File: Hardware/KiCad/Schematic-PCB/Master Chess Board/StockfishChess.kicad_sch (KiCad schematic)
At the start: 70 parts, among them J1 ZF1-15-02-X-WT-X, J2 USB4110GFA, J4 ZF1-15-02-X-WT-X, J6 ZF1-15-02-X-WT-X, J8 ZF1-15-02-X-WT-X, SW2 SW_Omron_B3FS, U1 ESP32-S3-WROOM-2, U143 SN74AHCT125D, U144 USBLC6-2P6, U145 RUEF300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

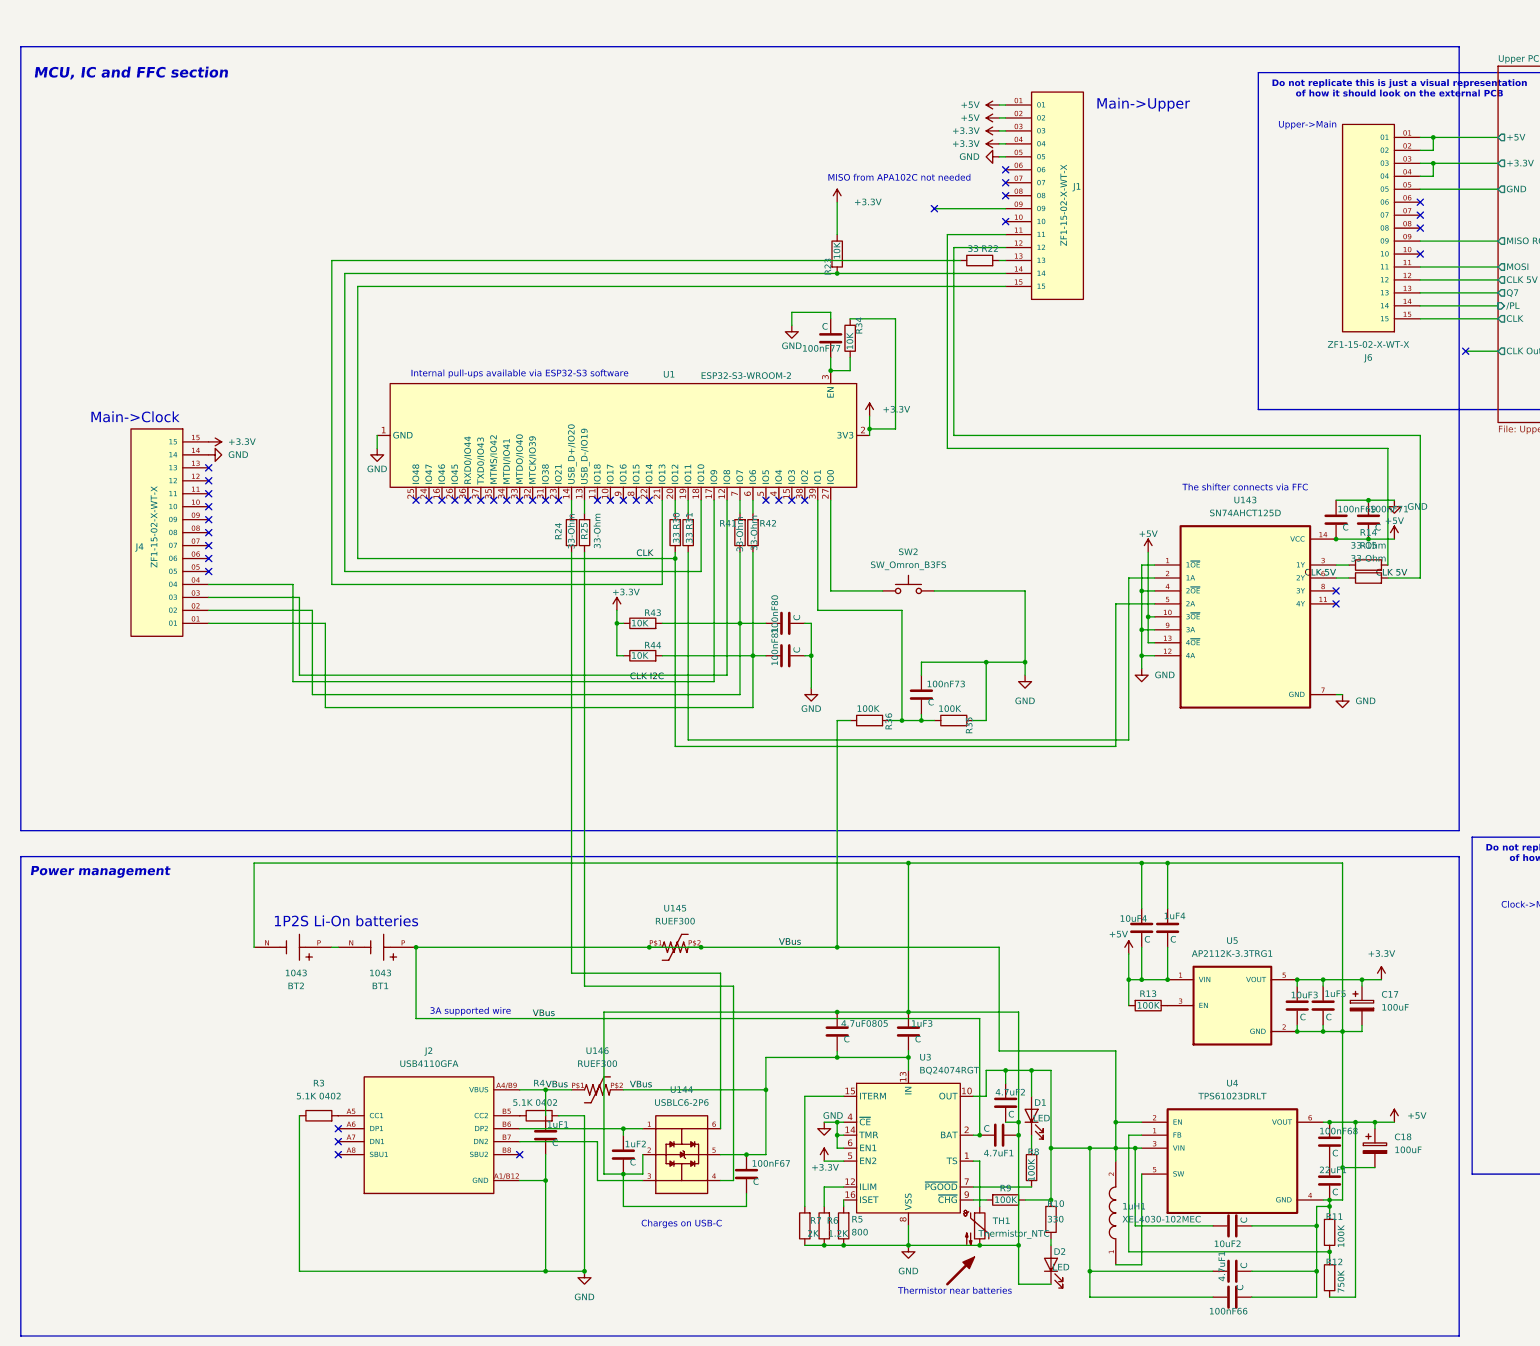
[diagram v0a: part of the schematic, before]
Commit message: Improved Schematic visuals
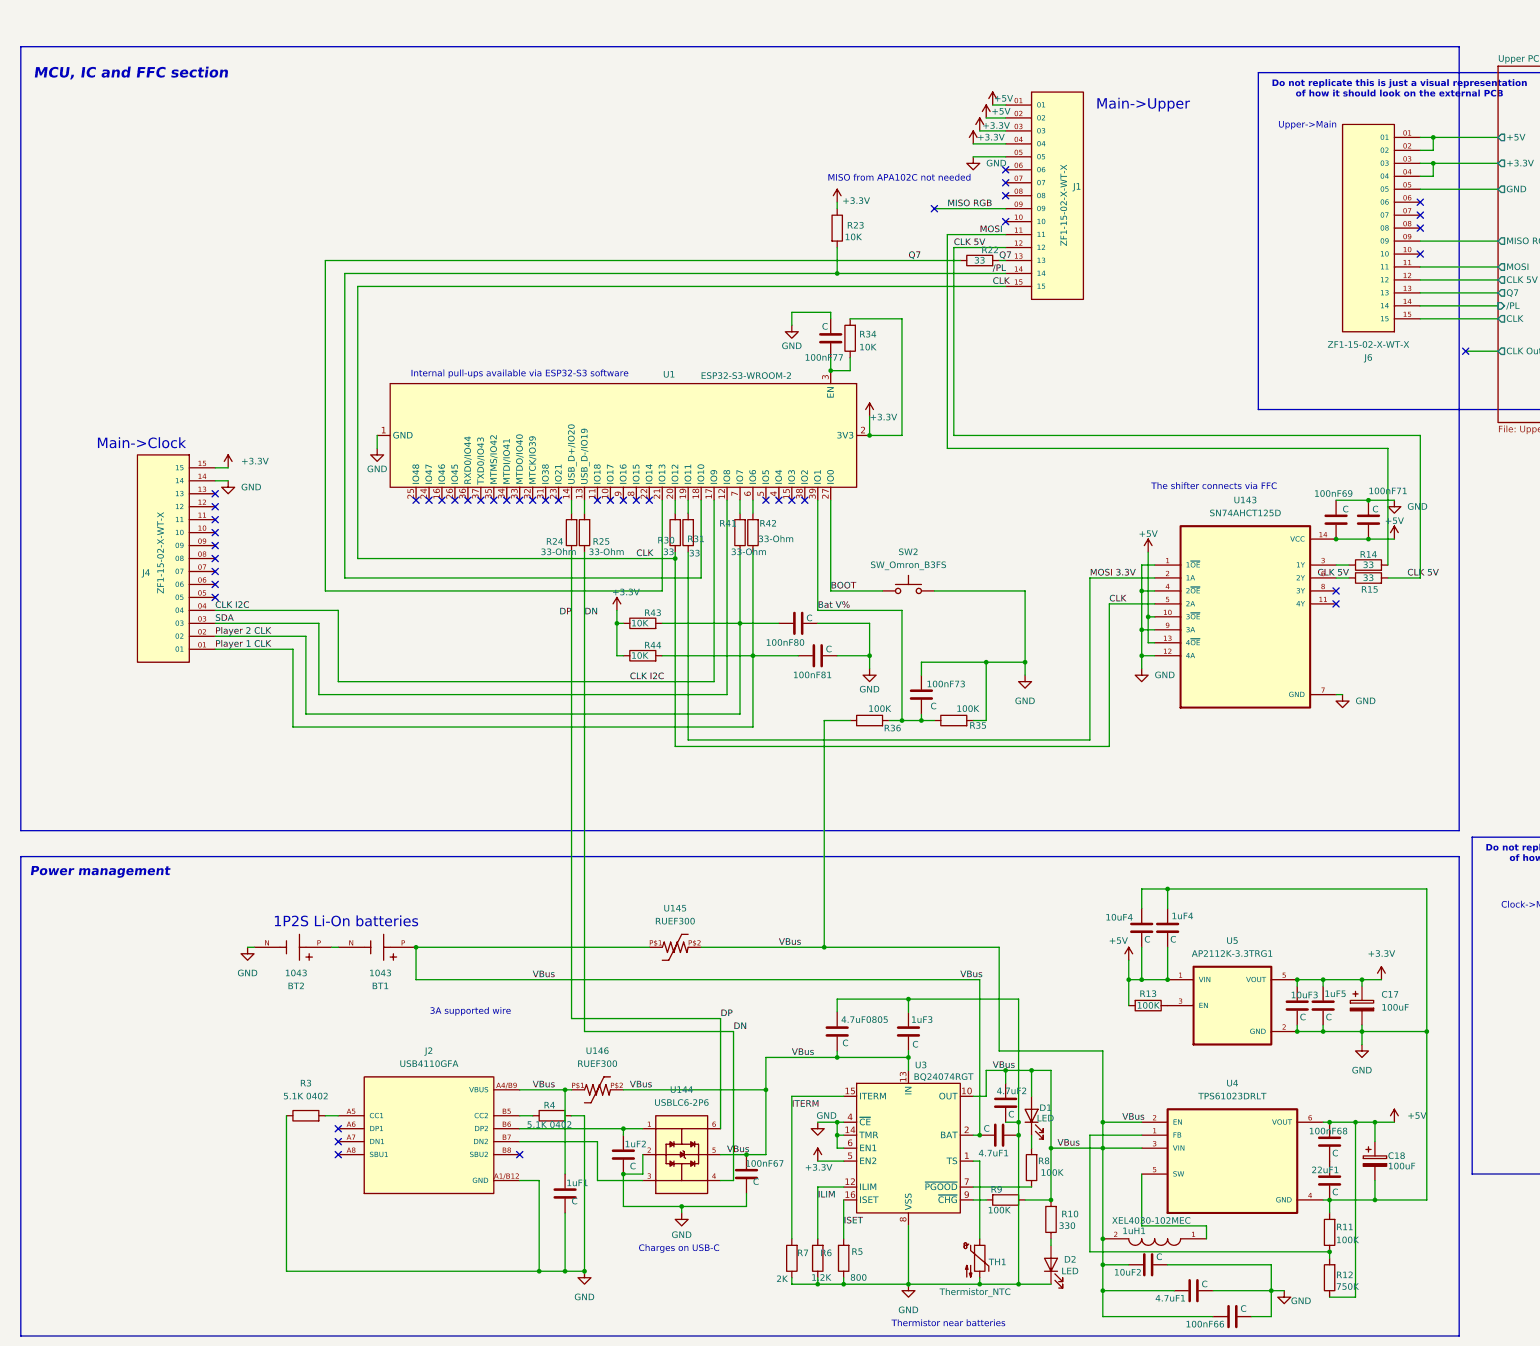
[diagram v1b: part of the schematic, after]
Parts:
- R14, R15: value 33-Ohm -> 33
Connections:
- net Q7: now reaches R22.1, U1.21 (IO13)
- net Q7: now also J1.13, R22.2
- net DN: now reaches R25.1, U144.4
- net ITERM: now reaches R7.2, U3.15 (ITERM)
- net SDA: now reaches J4.03, U1.12 (IO8)
- net /PL: now reaches J1.14, R23.2, U1.18 (IO10)
- net BOOT: now reaches SW2.1, U1.27 (IO0)
- net Bat V%: now reaches 100nF73.2, R35.1, R36.2, U1.39 (IO1)
- net DP: now reaches R24.1, U144.6
- net MOSI 3.3V: now reaches R31.1, U143.2 (1A)
- net ISET: now reaches R5.2, U3.16 (ISET)
- net Player 2 CLK: now reaches 100nF80.1, J4.02, R41.1, R43.2
- net ILIM: now reaches R6.2, U3.12 (ILIM)
- net Player 1 CLK: now reaches 100nF81.1, J4.01, R42.1, R44.2
- net MOSI: now reaches J1.11, R14.2
- net MISO RGB: now reaches J1.09
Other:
- moved on the sheet: 100nF66, 100nF80, 100nF81, 10uF2, 1uF1, 1uH1, 4.7uF1, C18, J4, R23, R3, R4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

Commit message: Added pulups to hall effect
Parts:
- removed 1uF2: C, symbol Device:C
- added 100nF1, 22uF4: C, symbol Device:C
- added R37: 3.3K, symbol Device:R
- added R38: 6.8K, symbol Device:R
- renumbered 4.7uF1 to 4.7uF3
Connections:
- net +3.3V: now also 100nF1.2, 22uF4.2
- net GND: now also BT1.N, 100nF1.1, 22uF4.1, R38.1
- net Q7: now also R37.1; no longer U1.21 (IO13)
- net VBUS: no longer 4.7uF1.2, BT1.P, U145.P$1, U3.2 (BAT), U3.3 (BAT)
- net BAT: now reaches BT2.P
- net BAT: now also 4.7uF1.2, BT1.P, U145.P$1, U3.2 (BAT), U3.3 (BAT); no longer BT1.N
- new net: R37.2, R38.2, U1.21 (IO13)
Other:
- note added: "2P1S Li-On batteries"
- note added: "Voltage divider 5V -> 3.3V"
- note removed: "1P2S Li-On batteries"
- moved on the sheet: BT2

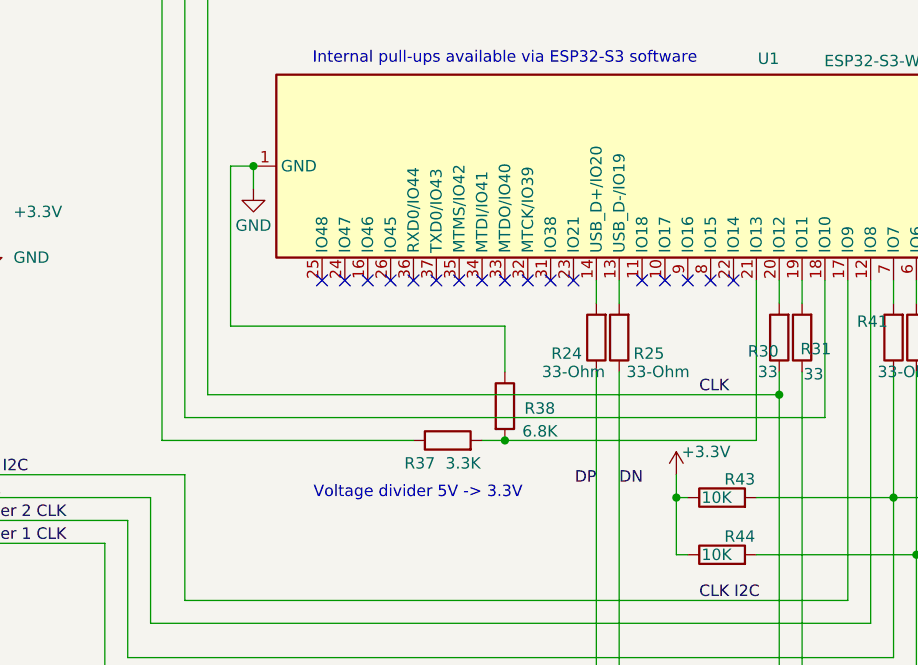
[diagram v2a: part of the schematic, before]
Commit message: Had an excess voltage divider
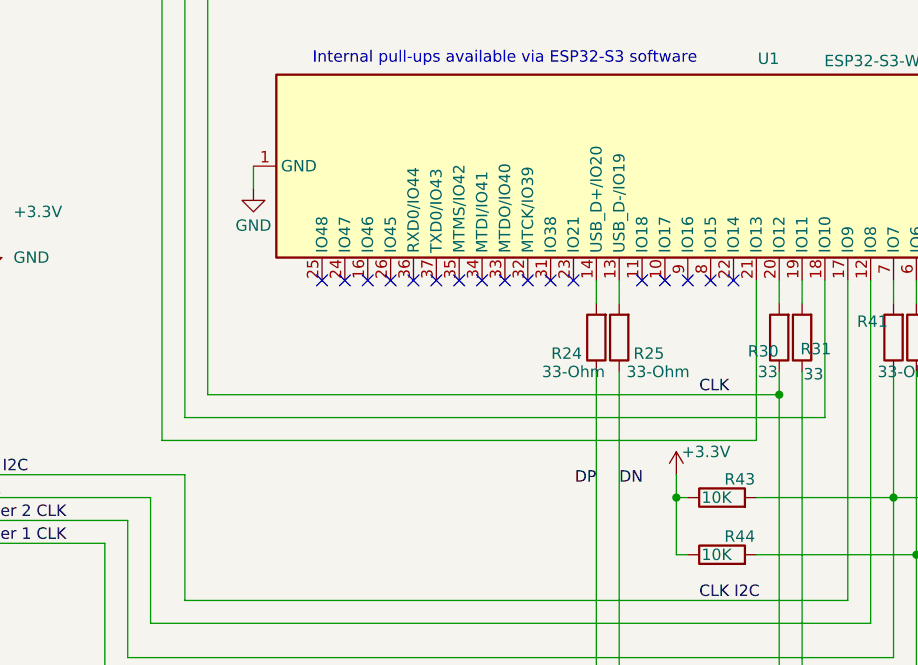
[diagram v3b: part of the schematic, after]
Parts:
- removed R37: 3.3K, symbol Device:R
- removed R38: 6.8K, symbol Device:R
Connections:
- net Q7: now also U1.21 (IO13)
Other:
- note removed: "Voltage divider 5V -> 3.3V"
